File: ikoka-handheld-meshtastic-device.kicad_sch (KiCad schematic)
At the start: 39 parts, among them J1 Conn_Coaxial, J4 1.25-2PWB, Q1 AO3401A, SW1 SW_Push, SW2 SW_Push, U1 MT3608B, U2 E22-900M30S, U3 XIAO-nRF52840-SMD, U4 TP4056-42-ESOP8

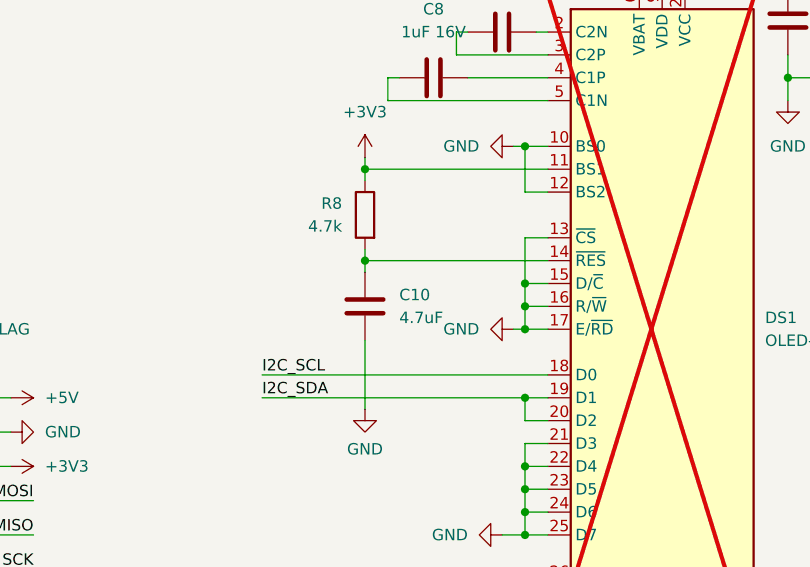
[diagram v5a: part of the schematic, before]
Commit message: fix: Add 4.7kΩ pull-up resistors on I2C bus (fixes #5)
Signed-off-by: Andrew Yong <me@ndoo.sg>
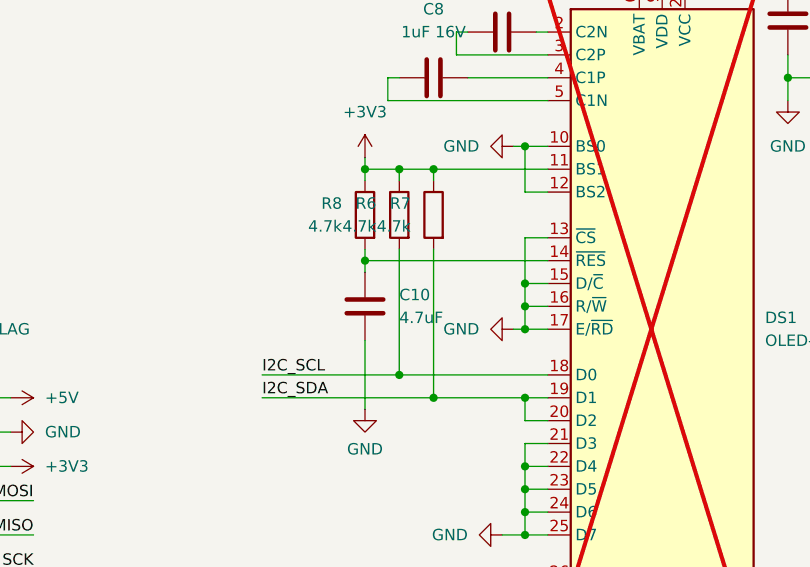
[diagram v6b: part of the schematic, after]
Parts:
- added R6, R7: 4.7k, Resistor_SMD:R_0603_1608Metric, symbol Device:R
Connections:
- net +3V3: now also R6.1, R7.1
- net I2C_SCL: now also R6.2
- net I2C_SDA: now also R7.2
